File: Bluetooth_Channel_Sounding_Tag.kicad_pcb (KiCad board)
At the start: 4 copper layers, 35 x 40 mm, 67 parts, among them CN1 S2B-PH-SM4-TB, J1 Conn_02x03_Odd_Even, Q1 MMBT3904-C20526, Q2 AO3401A, Q3 DMN2056U-7, SW1 TS-1088-AR02016, U1 NPM1300-QEAA-R7, U2 NRF54L15-QFAA-R, U3 BGS 12WN6 E6327, U4 LIS2DW12TR, X1 32MHz, X2 32.768KHz

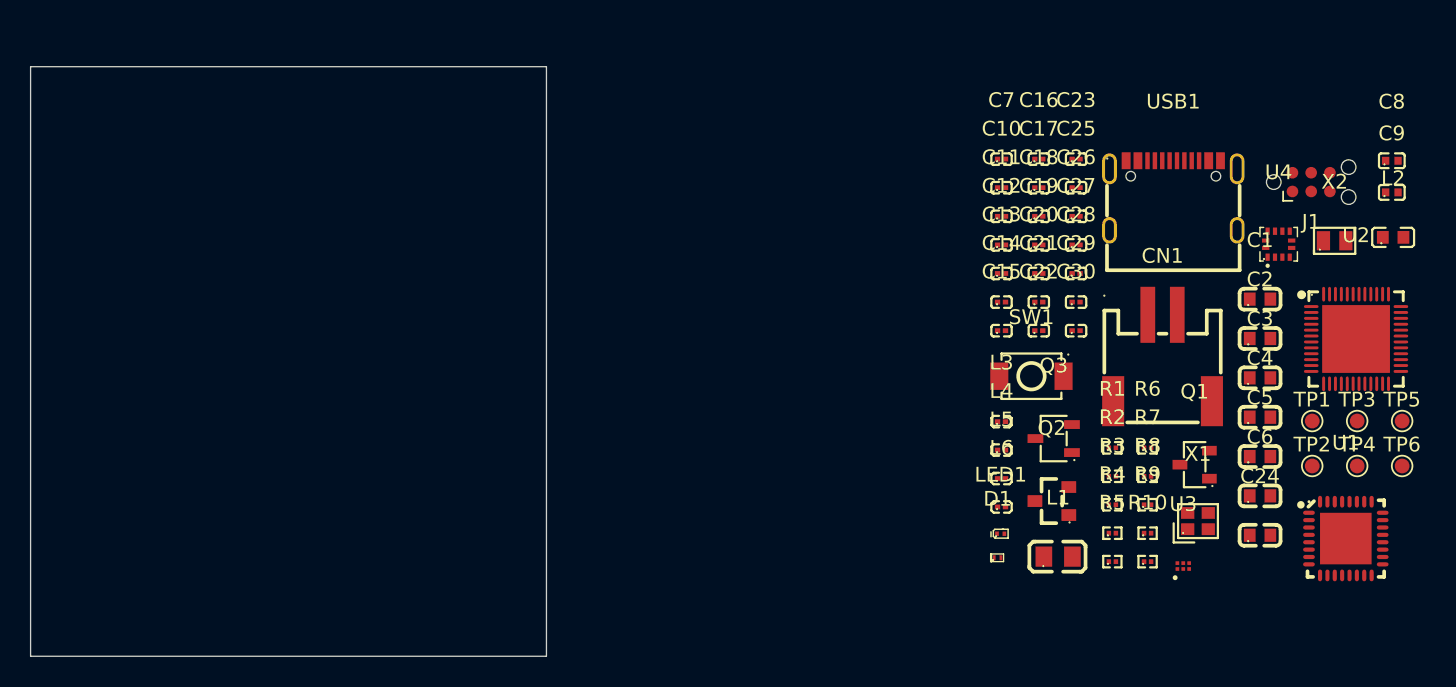
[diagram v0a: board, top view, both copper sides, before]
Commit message: Place components and start routing the PCB
Expand the board to 35 x 42.5 mm with 2 mm rounded corners. Add the M2
mounting hole and two antenna reservations, and arrange the power, MCU,
sensor, RF and programming components.

Add initial routing for the USB input, battery protection, PMIC power
connections, I2C, button, testpoints and 32 kHz crystal. Reposition L1 and
C6 to shorten the BUCK1 switch connection and improve the output routing.
Include the updated project settings and repositioned schematic drawing.

This is an in-progress layout checkpoint. Ground planes and returns,
remaining supply and bus connections, debug, the 32 MHz crystal and RF
and antenna routing still need work. ERC and DRC were not run for this
checkpoint.
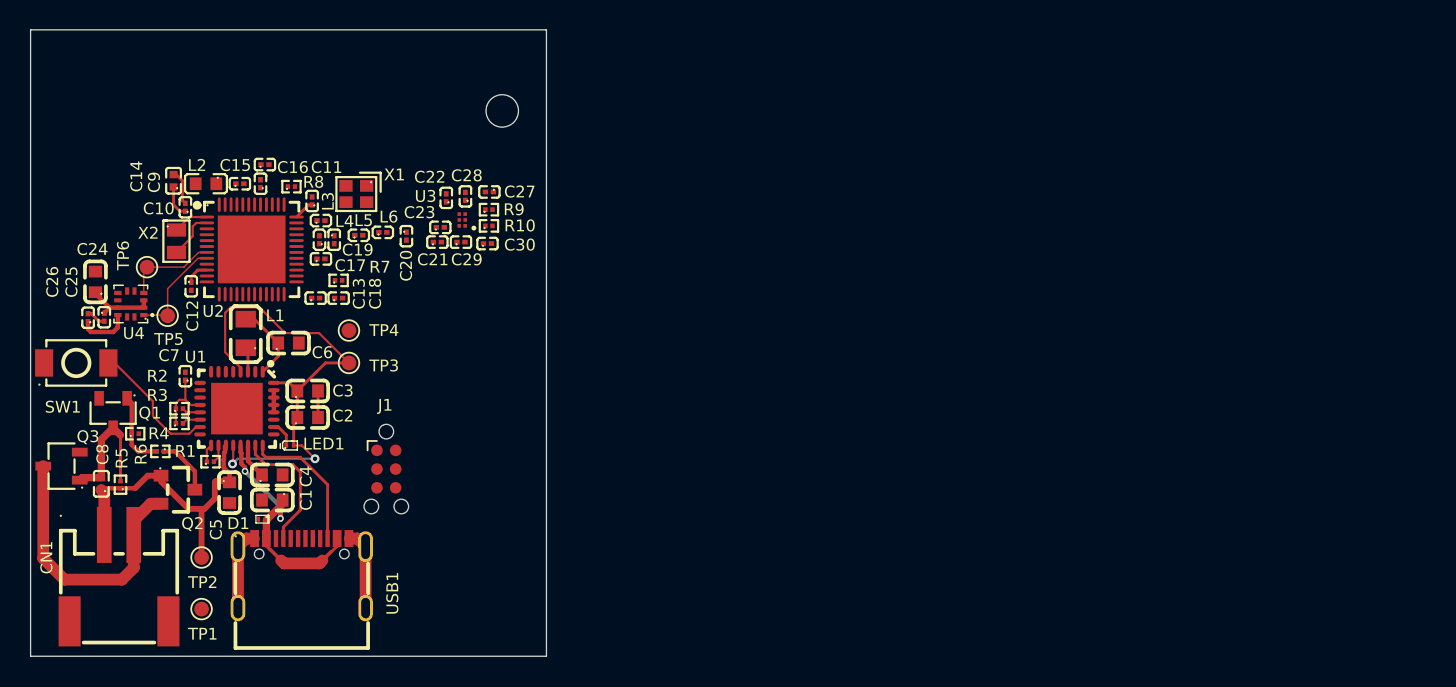
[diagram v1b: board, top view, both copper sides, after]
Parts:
- added H1: MountingHole_2.2mm_M2, MountingHole:MountingHole_2.2mm_M2, F.Cu at (142.5, 83.4)
- moved C8 90.3 mm to (115.3, 108.7), turned to 90 degrees
- moved TP6 86.2 mm to (118.4, 94.0)
- moved TP5 84.1 mm to (119.8, 97.3)
- moved C9 82.7 mm to (120.2, 88.1), turned to 90 degrees
- moved C24 80.9 mm to (114.9, 95.0), turned to 90 degrees
- moved L2 80.6 mm to (122.4, 88.3), turned to 180 degrees
- moved X2 78.6 mm to (120.4, 92.2), turned to -90 degrees
- moved U4 78.0 mm to (117.3, 96.5), turned to 90 degrees
- moved TP1 76.4 mm to (122.1, 117.2)
- moved U1 75.7 mm to (124.5, 103.6), turned to -90 degrees
- moved TP2 75.6 mm to (122.1, 113.7)
- moved U2 75.2 mm to (125.5, 92.8)
- moved Q1 73.5 mm to (116.1, 103.9), turned to 90 degrees
- moved CN1 72.4 mm to (116.5, 115.1)
- moved C5 70.0 mm to (124.0, 109.3), turned to -90 degrees
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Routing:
- net /VSYS: track 0.00 -> 33.3 mm, vias 0 -> 2
- net /VOUT1: track 0.00 -> 23.4 mm
- net /VBAT: track 0.00 -> 20.8 mm
- net GND: track 0.00 -> 19.2 mm
- net Net-(CN1-Pad2): track 0.00 -> 18.9 mm
- net Net-(U1-VBUS): track 0.00 -> 17.3 mm, vias 0 -> 2
- net /CC2: track 0.00 -> 9.51 mm
- net /CC1: track 0.00 -> 9.13 mm
- net Net-(C8-Pad2): track 0.00 -> 9.07 mm
- net /SHPHLD: track 0.00 -> 8.98 mm
- net /SCL: track 0.00 -> 8.33 mm
- net /SDA: track 0.00 -> 7.58 mm
- net Net-(Q1-Pad1): track 0.00 -> 5.17 mm
- net Net-(Q2-Pad3): track 0.00 -> 3.95 mm
- net Net-(U2-P1.01/XL2): track 0.00 -> 3.28 mm
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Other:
- board size 35 x 40 mm -> 35 x 42.5 mm

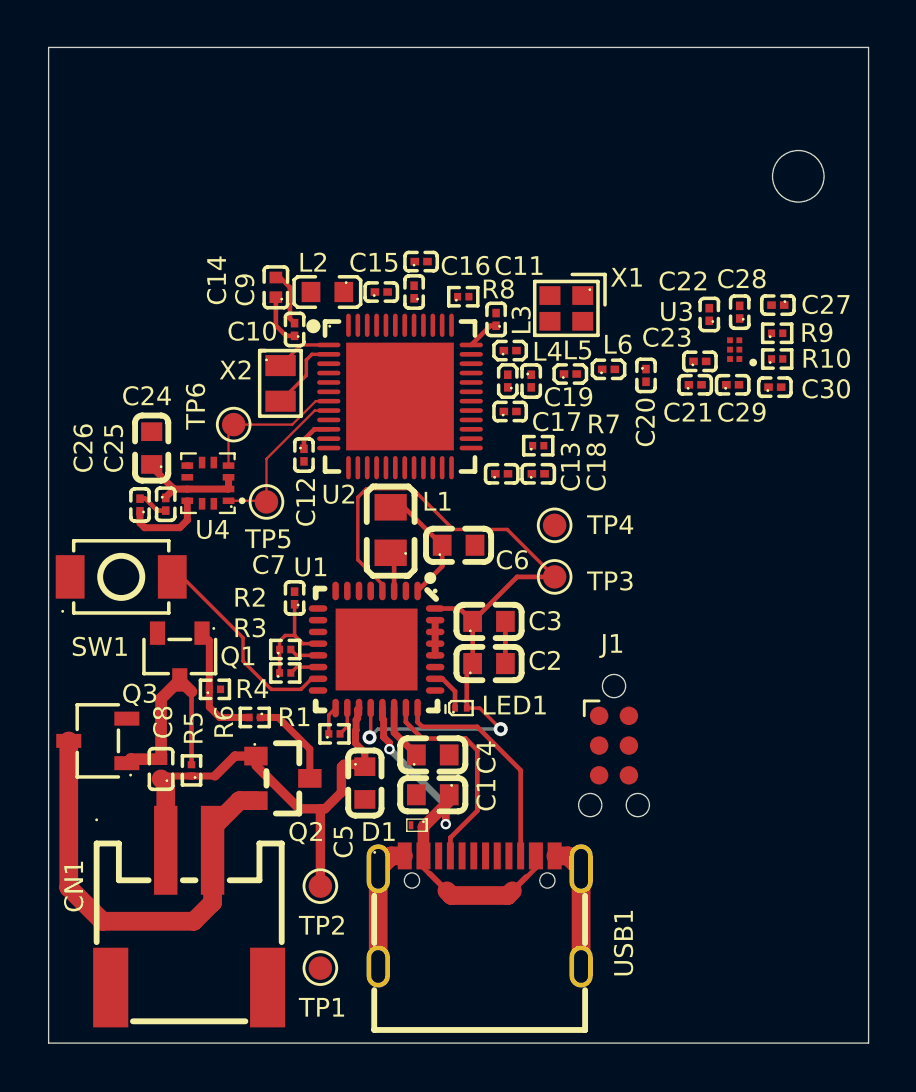
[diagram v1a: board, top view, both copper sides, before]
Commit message: Route the RF paths and add PhaseTag branding
Add ground pours and RF grounding, route both PCB antennas through the RF switch, and define the 50-ohm RF routing profile.

Refine power, signal and debugger routing, assign the antenna footprints in the schematic, and add the PhaseTag logo, product name, designer credit and revision marking.
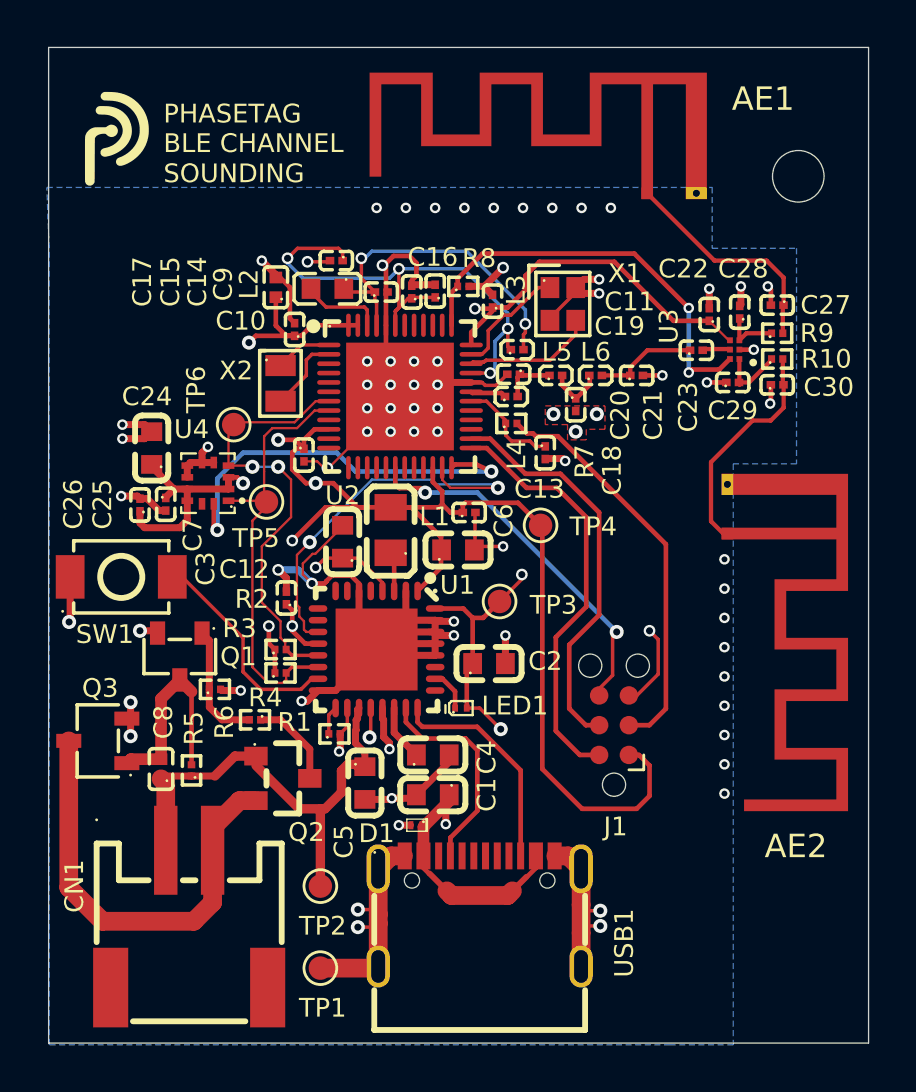
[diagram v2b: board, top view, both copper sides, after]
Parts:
- added AE1: TI_AN043_IFA, RF_Antenna:Texas_SWRA117D_2.4GHz_Left, F.Cu at (136.1, 84.1)
- added AE2: TI_AN043_IFA, RF_Antenna:Texas_SWRA117D_2.4GHz_Right, F.Cu at (139.5, 98.7)
- added G***: LOGO, BCS:PhaseTag_Logo, F.Cu at (113.2, 81.8)
- moved C17 9.82 mm to (122.8, 87.0), turned to 180 degrees
- moved C3 7.11 mm to (123.0, 99.0), turned to 90 degrees
- moved C20 3.25 mm to (133.0, 93.2)
- moved TP3 2.57 mm to (129.8, 101.5)
- moved C21 2.53 mm to (135.6, 91.9)
- moved C13 2.16 mm to (128.4, 97.8)
- moved R7 1.49 mm to (130.2, 94.0)
- moved C16 1.40 mm to (127.0, 88.3), turned to 90 degrees
- moved C18 0.95 mm to (131.7, 95.2), turned to -90 degrees
- moved J1 0.87 mm to (134.6, 106.8), turned to 90 degrees
- moved C19 0.80 mm to (130.3, 91.8), turned to 180 degrees
- moved C11 0.79 mm to (129.4, 88.7)
- moved L4 0.68 mm to (130.2, 92.8), turned to 0 degrees
- moved L5 0.62 mm to (132.2, 91.9)
- moved L6 0.61 mm to (133.8, 91.9)
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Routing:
- net GND: track 19.2 -> 114.5 mm, vias 0 -> 76
- net /VOUT1: track 23.4 -> 107.5 mm, vias 0 -> 8
- net Net-(U2-DECA): track 0.00 -> 22.9 mm, vias 0 -> 4
- net /ANT_SEL: track 0.00 -> 18.1 mm, vias 0 -> 2
- net /SWDIO: track 0.00 -> 18.1 mm
- net /ACCEL_INT: track 0.00 -> 17.7 mm, vias 0 -> 2
- net /NRESET: track 0.00 -> 17.4 mm
- net /SWDCLK: track 0.00 -> 17.2 mm
- net /PMIC_INT: track 0.00 -> 17.1 mm, vias 0 -> 2
- net /SWO: track 0.00 -> 15.8 mm, vias 0 -> 2
- net /DECD: track 0.00 -> 14.4 mm, vias 0 -> 2
- net /SDA: track 7.58 -> 18.7 mm, vias 0 -> 2
- net /SCL: track 8.33 -> 18.4 mm
- net Net-(AE1-A): track 0.00 -> 9.67 mm
- net Net-(AE2-A): track 0.00 -> 9.63 mm
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- added copper zone on B.Cu, net GND
- added copper zone on F.Cu, net GND
- added copper zone on In1.Cu, net GND
- added copper zone on In2.Cu, net GND
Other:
- board text added: "BLE CHANNEL SOUNDING"
- board text added: "Designed by Yafet Daniel REV A | 2026-10"
- board text added: "PHASETAG"

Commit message: Refine board annotations and organize logo assets
Add 35 x 42.5 mm board dimensions on the drawing layer and adjust the crystal placement and component reference labels. Rename Branding to logo and retain the current project settings.
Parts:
- moved X1 0.10 mm to (132.6, 88.8)
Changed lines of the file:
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@@
 		(at 130.5 90.8)
 		(property "Reference" "L3"
-			(at -0.05 -2.55 90)
+			(at 0 -2.55 90)
 			(layer "F.SilkS")
 			(effects
@@
 	(footprint "BCS:CRYSTAL-SMD_4P-L2.0-W1.6-BL"
 		(layer "F.Cu")
-		(at 132.45 88.85 -90)
+		(at 132.55 88.85 -90)
 		(property "Reference" "X1"
 			(at -1.3 -2.65 180)
@@
 		(tags "test point SMD pad")
 		(property "Reference" "TP1"
-			(at 0.1 1.7 0)
+			(at 0.1 1.8 0)
 			(layer "F.SilkS")
 			(effects
@@
 		(at 125.5 92.8)
 		(property "Reference" "U2"
-			(at -2.45 4.225 0)
+			(at 3.1 3.9 0)
 			(layer "F.SilkS")
 			(effects
@@
 		)
 	)
+	(dimension
+		(type orthogonal)
+		(layer "Dwgs.User")
+		(pts
+			(xy 110.5 118.5) (xy 145.5 118.5)
+		)
+		(height 5.4)
+		(orientation 0)
+		(format
+			(prefix "")
+			(suffix "")
+			(units 3)
+			(units_format 0)
+			(precision 4)
+			(suppress_zeroes yes)
+		)
+		(style
+			(thickness 0.1)
+			(arrow_length 1.27)
+			(text_position_mode 0)
+			(arrow_direction outward)
+			(extension_height 0.58642)
+			(extension_offset 0.5)
+			(keep_text_aligned yes)
+		)
+		(gr_text "35"
+			(at 128 122.75 0)
+			(layer "Dwgs.User")
+			(effects
+				(font
+					(size 1 1)
+					(thickness 0.15)
+				)
+			)
+		)
+	)
+	(dimension
+		(type orthogonal)
+		(layer "Dwgs.User")
+		(pts
+			(xy 142.1 77.9) (xy 142.1 120.4)
+		)
+		(height 7)
+		(orientation 1)
+		(format
+			(prefix "")
+			(suffix "")
+			(units 3)
+			(units_format 0)
+			(precision 4)
+			(suppress_zeroes yes)
+		)
+		(style
+			(thickness 0.1)
+			(arrow_length 1.27)
+			(text_position_mode 0)
+			(arrow_direction outward)
+			(extension_height 0.58642)
+			(extension_offset 0.5)
+			(keep_text_aligned yes)
+		)
+		(gr_text "42.5"
+			(at 147.95 99.15 90)
+			(layer "Dwgs.User")
+			(effects
+				(font
+					(size 1 1)
+					(thickness 0.15)
+				)
+			)
+		)
+	)
